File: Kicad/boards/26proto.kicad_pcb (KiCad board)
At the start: 2 copper layers, 98.8 x 93.1 mm, 60 parts, among them J1 5051104096, J10 Conn_01x05, J2 Micro_SD_Card, J3 URM37, J4 RE12A, J5 RS485_TFT, J6 RS485_airdata, J7 RS485_logger_2, J8 RS485_logger, J9 BNO085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

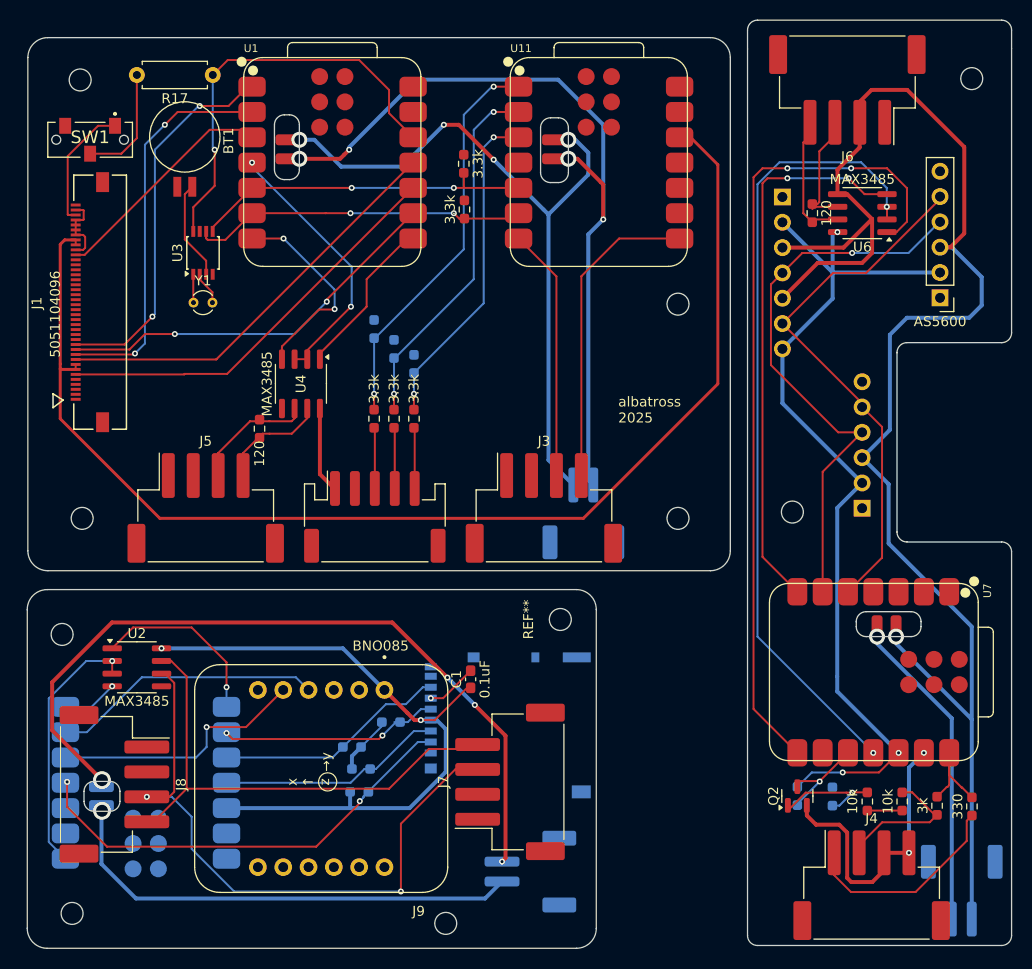
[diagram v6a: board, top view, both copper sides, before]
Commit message: added LED
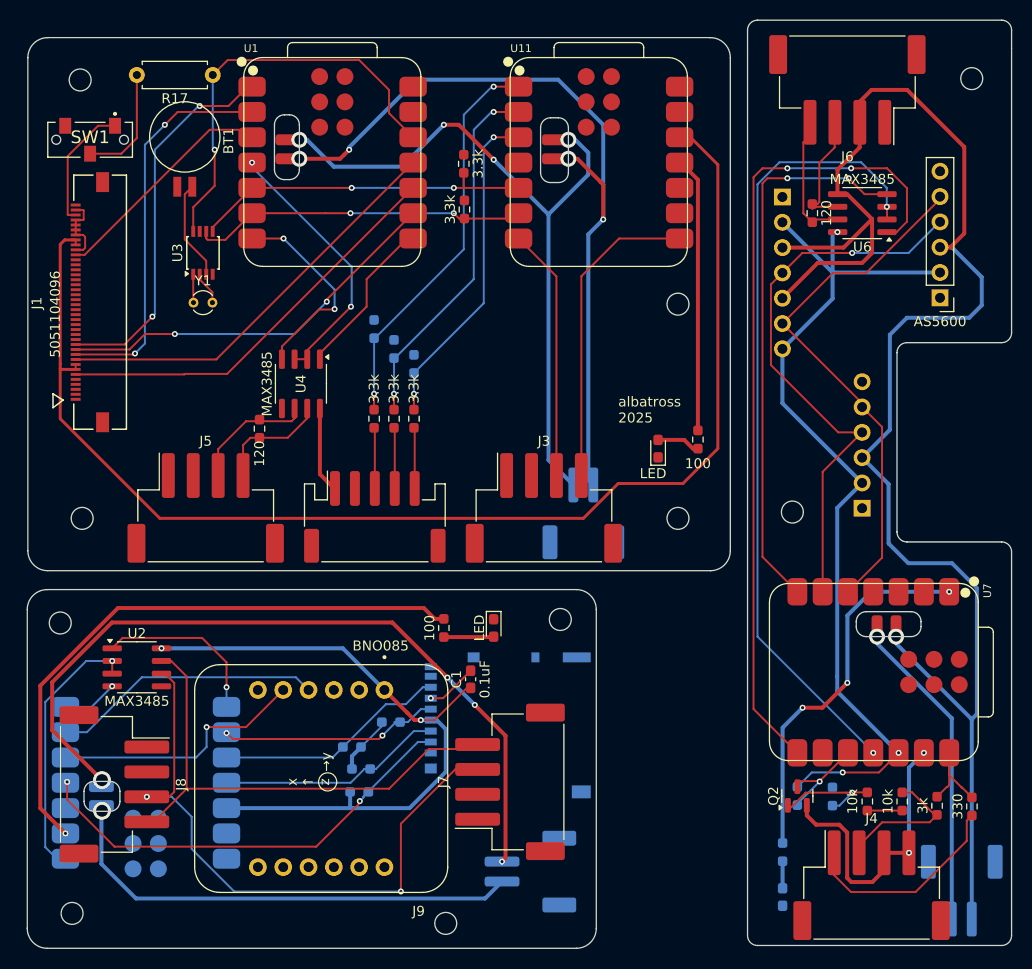
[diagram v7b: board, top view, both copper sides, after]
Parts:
- added D1: LED, LED_SMD:LED_0603_1608Metric_Pad1.05x0.95mm_HandSolder, F.Cu at (207.5, 70.0)
- added D2: LED, LED_SMD:LED_0603_1608Metric_Pad1.05x0.95mm_HandSolder, F.Cu at (191.0, 88.0)
- added D3: LED, LED_SMD:LED_0603_1608Metric_Pad1.05x0.95mm_HandSolder, B.Cu at (220.0, 115.0)
- added R22: 100, Resistor_SMD:R_0603_1608Metric_Pad0.98x0.95mm_HandSolder, F.Cu at (186.0, 88.0)
- added R23: 100, Resistor_SMD:R_0603_1608Metric_Pad0.98x0.95mm_HandSolder, F.Cu at (211.5, 69.1)
- added R24: 100, Resistor_SMD:R_0603_1608Metric_Pad0.98x0.95mm_HandSolder, B.Cu at (220.0, 110.5)
- moved REF** 1.16 mm to (147.5, 87.5)
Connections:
- U11 pad 11: unconnected-(U11-GPIO10_D10_MOSI-Pad11) -> Net-(U11-GPIO10_D10_MOSI)
- U5 pad 2: unconnected-(U5-GPIO3_A1_D1-Pad2) -> Net-(U5-GPIO3_A1_D1)
- U7 pad 1: unconnected-(U7-GPIO2_A0_D0-Pad1) -> Net-(U7-GPIO2_A0_D0)
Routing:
- net Net-(U5-GPIO3_A1_D1): track 0.00 -> 60.1 mm, vias 0 -> 1
- net Net-(U7-GPIO2_A0_D0): track 0.00 -> 37.9 mm, vias 0 -> 3
- net Net-(U11-GPIO10_D10_MOSI): track 0.00 -> 27.7 mm
- net Net-(D2-A): track 0.00 -> 5.02 mm
- net Net-(D1-A): track 0.00 -> 4.36 mm
- net pot_Vin: track 340.5 -> 344.3 mm
- net encoder_cathode: track 316.8 -> 319.8 mm
- net Net-(D3-A): track 0.00 -> 2.71 mm
- net Net-(U2-RO): track 18.3 -> 17.4 mm
- net Net-(U2-DE): track 26.0 -> 26.8 mm
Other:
- board text added: "①"
- board text added: "②"
- board text added: "③"

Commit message: added jumper
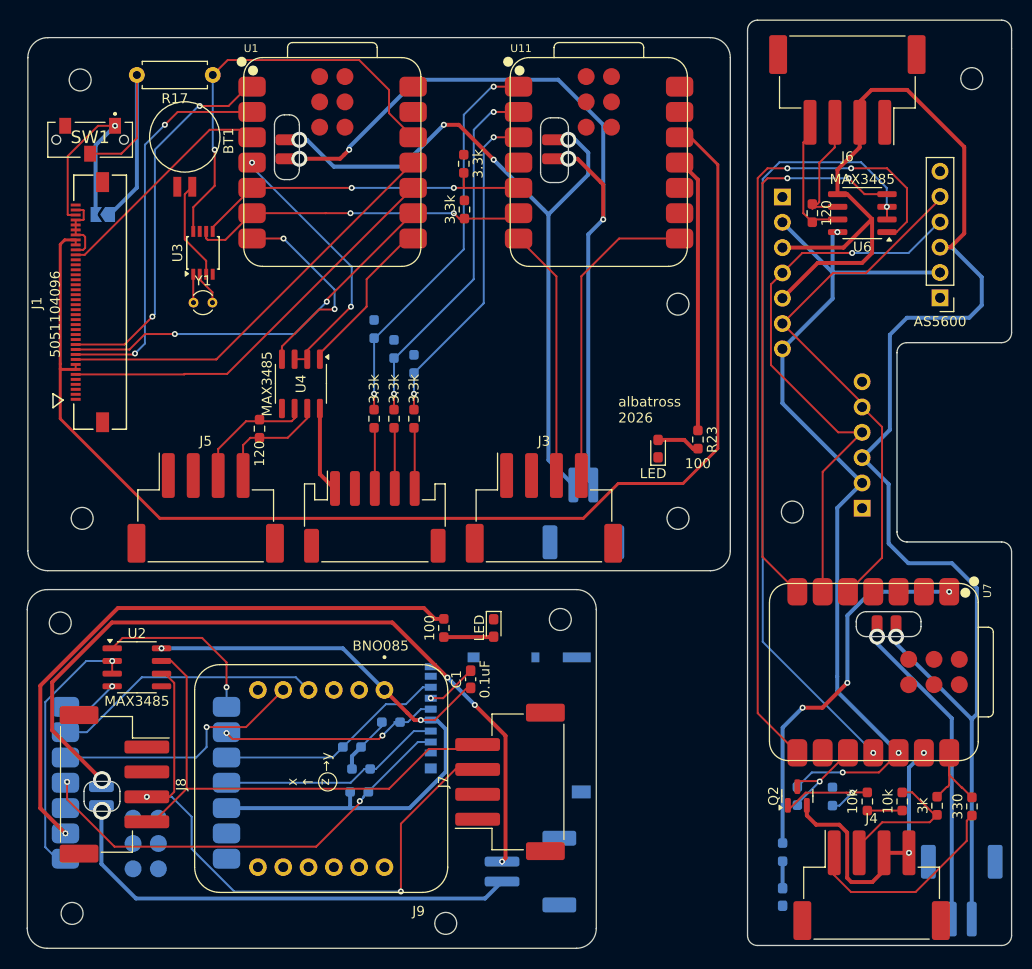
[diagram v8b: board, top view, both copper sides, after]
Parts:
- added JP1: SolderJumper_2_Open, Jumper:SolderJumper-2_P1.3mm_Open_TrianglePad1.0x1.5mm, B.Cu at (151.8, 46.5)
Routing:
- net Net-(JP1-A): track 11.7 -> 26.8 mm
- net Net-(JP1-B): track 12.7 -> 22.4 mm, vias 0 -> 1
- net Net-(U6-RO): track 82.0 -> 81.3 mm
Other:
- board text added: "albatross 2026"
- board text removed: "albatross 2025"
